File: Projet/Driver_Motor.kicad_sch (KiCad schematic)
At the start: 7 parts

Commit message: board_schematic
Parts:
- removed JP?: SolderJumper_2_Open, symbol Jumper:SolderJumper_2_Open
- added JP?: SolderJumper_2_Open, Jumper:SolderJumper-2_P1.3mm_Open_TrianglePad1.0x1.5mm, symbol Jumper:SolderJumper_2_Open
- JP3002: renamed from JP?; footprint (none) -> Jumper:SolderJumper-2_P1.3mm_Open_TrianglePad1.0x1.5mm
- gave numbers to parts that had none: 5
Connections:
- net +3.3V: now also U3001.3 (VDD)
- net V+_batterie: now also JP?.2 (B); no longer U3001.2 (VM)
- new net: JP?.1 (A), U3001.2 (VM)

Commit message: pcb_begin
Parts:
- removed JP?: SolderJumper_2_Open, Jumper:SolderJumper-2_P1.3mm_Open_TrianglePad1.0x1.5mm, symbol Jumper:SolderJumper_2_Open
- added JP302, JP303: SolderJumper_2_Open, Jumper:SolderJumper-2_P1.3mm_Open_TrianglePad1.0x1.5mm, symbol Jumper:SolderJumper_2_Open
- J301: renamed from J3001; footprint Connector_JST:JST_XH_B6B-XH-AM_1x06_P2.50mm_Vertical -> Connector_JST:JST_XH_B6B-XH-A_1x06_P2.50mm_Vertical
- J302: renamed from J3002; footprint Connector_JST:JST_XH_B6B-XH-AM_1x06_P2.50mm_Vertical -> Connector_JST:JST_XH_B6B-XH-A_1x06_P2.50mm_Vertical
- U301: renamed from U3001; footprint Package_SO:SOIC-8_3.9x4.9mm_P1.27mm -> Package_SO:SO-8_3.9x4.9mm_P1.27mm
- U302: renamed from U3002; footprint Package_SO:SOIC-8_3.9x4.9mm_P1.27mm -> Package_SO:SO-8_3.9x4.9mm_P1.27mm
- renumbered J3003 to J303, JP3002 to JP301
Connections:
- net +3.3V: now also JP302.2 (B); no longer U301.3 (VDD)
- net V+_batterie: now also JP303.2 (B)
- net at U301.2 (VM): now also JP303.1 (A)
- new net: JP302.1 (A), U301.3 (VDD)
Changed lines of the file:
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@@
     (stroke (width 0) (type default) (color 0 0 0 0))
   )
-  (wire (pts (xy 50.8 133.604) (xy 50.8 144.78))
+  (wire (pts (xy 50.8 133.604) (xy 50.8 135.128))
     (stroke (width 0) (type default) (color 0 0 0 0))
   )
@@
   )
   (wire (pts (xy 54.61 28.956) (xy 54.61 32.004))
+    (stroke (width 0) (type default) (color 0 0 0 0))
+  )
+  (wire (pts (xy 50.8 142.748) (xy 50.8 144.78))
     (stroke (width 0) (type default) (color 0 0 0 0))
   )
@@
   (symbol (lib_id "Connector_Generic:Conn_01x06") (at 114.3 50.8 0) (unit 1)
     (in_bom yes) (on_board yes) (fields_autoplaced)
-    (property "Reference" "J3002" (id 0) (at 116.84 50.7999 0)
+    (property "Reference" "J302" (id 0) (at 116.84 50.7999 0)
       (effects (font (size 1.27 1.27)) (justify left))
     )
@@
       (effects (font (size 1.27 1.27)) (justify left))
     )
-    (property "Footprint" "Connector_JST:JST_XH_B6B-XH-AM_1x06_P2.50mm_Vertical" (id 2) (at 114.3 50.8 0)
+    (property "Footprint" "Connector_JST:JST_XH_B6B-XH-A_1x06_P2.50mm_Vertical" (id 2) (at 114.3 50.8 0)
       (effects (font (size 1.27 1.27)) hide)
     )
@@
     (pin "6")
   )
+  (symbol (lib_id "Jumper:SolderJumper_2_Open") (at 55.88 135.382 90) (unit 1)
+    (in_bom yes) (on_board yes) (fields_autoplaced)
+    (property "Reference" "JP303" (id 0) (at 58.42 134.1119 90)
+      (effects (font (size 1.27 1.27)) (justify right))
+    )
+    (property "Value" "SolderJumper_2_Open" (id 1) (at 58.42 136.6519 90)
+      (effects (font (size 1.27 1.27)) (justify right))
+    )
+    (property "Footprint" "Jumper:SolderJumper-2_P1.3mm_Open_TrianglePad1.0x1.5mm" (id 2) (at 55.88 135.382 0)
+      (effects (font (size 1.27 1.27)) hide)
+    )
+    (property "Datasheet" "~" (id 3) (at 55.88 135.382 0)
+      (effects (font (size 1.27 1.27)) hide)
+    )
+    (pin "1")
+    (pin "2")
+  )
   (symbol (lib_id "power:GND") (at 57.15 59.69 0) (unit 1)
     (in_bom yes) (on_board yes) (fields_autoplaced)
-    (property "Reference" "#PWR0116" (id 0) (at 57.15 66.04 0)
+    (property "Reference" "#PWR0304" (id 0) (at 57.15 66.04 0)
       (effects (font (size 1.27 1.27)) hide)
     )
@@
   (symbol (lib_id "Driver_Motor:ZXBM5210-S") (at 53.34 154.94 0) (unit 1)
     (in_bom yes) (on_board yes) (fields_autoplaced)
-    (property "Reference" "U3001" (id 0) (at 55.3594 162.56 0)
+    (property "Reference" "U301" (id 0) (at 55.3594 162.56 0)
       (effects (font (size 1.27 1.27)) (justify left))
     )
@@
       (effects (font (size 1.27 1.27)) (justify left))
     )
-    (property "Footprint" "Package_SO:SOIC-8_3.9x4.9mm_P1.27mm" (id 2) (at 54.61 161.29 0)
+    (property "Footprint" "Package_SO:SO-8_3.9x4.9mm_P1.27mm" (id 2) (at 54.61 161.29 0)
       (effects (font (size 1.27 1.27)) hide)
     )
@@
   (symbol (lib_id "power:+3.3V") (at 101.6 55.88 90) (unit 1)
     (in_bom yes) (on_board yes) (fields_autoplaced)
-    (property "Reference" "#PWR0123" (id 0) (at 105.41 55.88 0)
+    (property "Reference" "#PWR0307" (id 0) (at 105.41 55.88 0)
       (effects (font (size 1.27 1.27)) hide)
     )
@@
   (symbol (lib_id "Driver_Motor:ZXBM5210-S") (at 57.15 52.07 0) (unit 1)
     (in_bom yes) (on_board yes) (fields_autoplaced)
-    (property "Reference" "U3002" (id 0) (at 59.1694 59.69 0)
+    (property "Reference" "U302" (id 0) (at 59.1694 59.69 0)
       (effects (font (size 1.27 1.27)) (justify left))
     )
@@
       (effects (font (size 1.27 1.27)) (justify left))
     )
-    (property "Footprint" "Package_SO:SOIC-8_3.9x4.9mm_P1.27mm" (id 2) (at 58.42 58.42 0)
+    (property "Footprint" "Package_SO:SO-8_3.9x4.9mm_P1.27mm" (id 2) (at 58.42 58.42 0)
       (effects (font (size 1.27 1.27)) hide)
     )
@@
   (symbol (lib_id "power:+3.3V") (at 92.71 160.02 90) (unit 1)
     (in_bom yes) (on_board yes) (fields_autoplaced)
-    (property "Reference" "#PWR0120" (id 0) (at 96.52 160.02 0)
+    (property "Reference" "#PWR0306" (id 0) (at 96.52 160.02 0)
       (effects (font (size 1.27 1.27)) hide)
     )
@@
     (pin "1")
   )
-  (symbol (lib_id "Jumper:SolderJumper_2_Open") (at 55.88 135.382 90) (unit 1)
-    (in_bom yes) (on_board yes) (fields_autoplaced)
-    (property "Reference" "JP?" (id 0) (at 58.42 134.1119 90)
-      (effects (font (size 1.27 1.27)) (justify right))
-    )
-    (property "Value" "SolderJumper_2_Open" (id 1) (at 58.42 136.6519 90)
-      (effects (font (size 1.27 1.27)) (justify right))
-    )
-    (property "Footprint" "Jumper:SolderJumper-2_P1.3mm_Open_TrianglePad1.0x1.5mm" (id 2) (at 55.88 135.382 0)
-      (effects (font (size 1.27 1.27)) hide)
-    )
-    (property "Datasheet" "~" (id 3) (at 55.88 135.382 0)
+  (symbol (lib_id "Jumper:SolderJumper_2_Open") (at 50.8 138.938 90) (unit 1)
+    (in_bom yes) (on_board yes) (fields_autoplaced)
+    (property "Reference" "JP302" (id 0) (at 53.34 137.6679 90)
+      (effects (font (size 1.27 1.27)) (justify right))
+    )
+    (property "Value" "SolderJumper_2_Open" (id 1) (at 53.34 140.2079 90)
+      (effects (font (size 1.27 1.27)) (justify right))
+    )
+    (property "Footprint" "Jumper:SolderJumper-2_P1.3mm_Open_TrianglePad1.0x1.5mm" (id 2) (at 50.8 138.938 0)
+      (effects (font (size 1.27 1.27)) hide)
+    )
+    (property "Datasheet" "~" (id 3) (at 50.8 138.938 0)
       (effects (font (size 1.27 1.27)) hide)
     )
@@
   (symbol (lib_id "power:GND") (at 102.87 48.26 270) (unit 1)
     (in_bom yes) (on_board yes) (fields_autoplaced)
-    (property "Reference" "#PWR0122" (id 0) (at 96.52 48.26 0)
+    (property "Reference" "#PWR0308" (id 0) (at 96.52 48.26 0)
       (effects (font (size 1.27 1.27)) hide)
     )
@@
   (symbol (lib_id "power:+3.3V") (at 54.61 28.956 0) (unit 1)
     (in_bom yes) (on_board yes) (fields_autoplaced)
-    (property "Reference" "#PWR0117" (id 0) (at 54.61 32.766 0)
+    (property "Reference" "#PWR0303" (id 0) (at 54.61 32.766 0)
       (effects (font (size 1.27 1.27)) hide)
     )
@@
   (symbol (lib_id "power:GND") (at 92.71 152.4 270) (unit 1)
     (in_bom yes) (on_board yes) (fields_autoplaced)
-    (property "Reference" "#PWR0115" (id 0) (at 86.36 152.4 0)
+    (property "Reference" "#PWR0305" (id 0) (at 86.36 152.4 0)
       (effects (font (size 1.27 1.27)) hide)
     )
@@
   (symbol (lib_id "Connector_Generic:Conn_01x06") (at 106.68 154.94 0) (unit 1)
     (in_bom yes) (on_board yes) (fields_autoplaced)
-    (property "Reference" "J3001" (id 0) (at 109.22 154.9399 0)
+    (property "Reference" "J301" (id 0) (at 109.22 154.9399 0)
       (effects (font (size 1.27 1.27)) (justify left))
     )
@@
       (effects (font (size 1.27 1.27)) (justify left))
     )
-    (property "Footprint" "Connector_JST:JST_XH_B6B-XH-AM_1x06_P2.50mm_Vertical" (id 2) (at 106.68 154.94 0)
+    (property "Footprint" "Connector_JST:JST_XH_B6B-XH-A_1x06_P2.50mm_Vertical" (id 2) (at 106.68 154.94 0)
       (effects (font (size 1.27 1.27)) hide)
     )
@@
   (symbol (lib_id "Connector_Generic:Conn_01x03") (at 199.39 95.25 0) (unit 1)
     (in_bom yes) (on_board yes) (fields_autoplaced)
-    (property "Reference" "J3003" (id 0) (at 201.93 93.9799 0)
+    (property "Reference" "J303" (id 0) (at 201.93 93.9799 0)
       (effects (font (size 1.27 1.27)) (justify left))
     )
@@
   (symbol (lib_id "power:GND") (at 194.31 92.71 270) (unit 1)
     (in_bom yes) (on_board yes) (fields_autoplaced)
-    (property "Reference" "#PWR0121" (id 0) (at 187.96 92.71 0)
+    (property "Reference" "#PWR0309" (id 0) (at 187.96 92.71 0)
       (effects (font (size 1.27 1.27)) hide)
     )
@@
   (symbol (lib_id "Jumper:SolderJumper_2_Open") (at 54.61 35.814 90) (unit 1)
     (in_bom yes) (on_board yes) (fields_autoplaced)
-    (property "Reference" "JP3002" (id 0) (at 57.15 34.5439 90)
+    (property "Reference" "JP301" (id 0) (at 57.15 34.5439 90)
       (effects (font (size 1.27 1.27)) (justify right))
     )
@@
   (symbol (lib_id "power:GND") (at 53.34 162.56 0) (unit 1)
     (in_bom yes) (on_board yes) (fields_autoplaced)
-    (property "Reference" "#PWR0118" (id 0) (at 53.34 168.91 0)
+    (property "Reference" "#PWR0302" (id 0) (at 53.34 168.91 0)
       (effects (font (size 1.27 1.27)) hide)
     )
@@
   (symbol (lib_id "power:+3.3V") (at 50.8 133.604 0) (unit 1)
     (in_bom yes) (on_board yes) (fields_autoplaced)
-    (property "Reference" "#PWR0119" (id 0) (at 50.8 137.414 0)
-      (effects (font (size 1.27 1.27)) hide)
-    )
+    (property "Reference" "#PWR0301" (id 0) (at 50.8 137.414 0)
+      (effects (font (size 1.27 1.27)) hide)
+    )

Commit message: placement
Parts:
- added C301: 100uF, Capacitor_THT:CP_Radial_D6.3mm_P2.50mm, symbol Device:C_Polarized_Small
- added C302: 0.1uF, Capacitor_SMD:C_0603_1608Metric_Pad1.08x0.95mm_HandSolder, symbol Device:C_Small
- added C303, C304: 1uF, Capacitor_SMD:C_0603_1608Metric_Pad1.08x0.95mm_HandSolder, symbol Device:C_Small
- added C305, C306: 100nF, Capacitor_SMD:C_0603_1608Metric_Pad1.08x0.95mm_HandSolder, symbol Device:C_Small
- added R301: 10k, Resistor_SMD:R_0603_1608Metric_Pad0.98x0.95mm_HandSolder, symbol Device:R_Small
- J303: footprint Connector_JST:JST_XH_S3B-XH-A_1x03_P2.50mm_Horizontal -> Connector_JST:JST_XH_B3B-XH-A_1x03_P2.50mm_Vertical
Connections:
- net +3.3V: now also R301.2
- net GND: now also C301.2, C302.1, C303.2, C304.2, C305.2, C306.2
- net SERV_DATA: now also R301.1
- net V+_batterie: now also C301.1, C302.2, C306.1
- net at JP303.1 (A), U301.2 (VM): now also C305.1
- net at JP302.1 (A), U301.3 (VDD): now also C303.1
- net at JP301.1 (A), U302.3 (VDD): now also C304.1
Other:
- moved on the sheet: JP303

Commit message: Routing
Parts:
- added C307, C308, C309, C310: 1uF, Capacitor_SMD:C_0603_1608Metric_Pad1.08x0.95mm_HandSolder, symbol Device:C_Small
- added JP304: SolderJumper_2_Open, Jumper:SolderJumper-2_P1.3mm_Open_TrianglePad1.0x1.5mm, symbol Jumper:SolderJumper_2_Open
- C305, C306: value 100nF -> 10uF
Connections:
- net +3.3V: no longer JP301.2 (B), JP302.2 (B)
- net GND: now also C307.1, C308.1, C309.1, C310.1
- net M1+: now also C310.2
- net M1-: now also C308.2
- net M2+: now also C309.2
- net M2-: now also C307.2
- net V+_batterie: now also JP304.2 (B); no longer C306.1, U302.2 (VM)
- new net: C306.1, JP304.1 (A), U302.2 (VM)
- new net +5V: JP301.2 (B), JP302.2 (B)
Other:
- note added: "Capacités 100 nF, recommandé pour faible courant"
- moved on the sheet: C301, C302, J301, J302

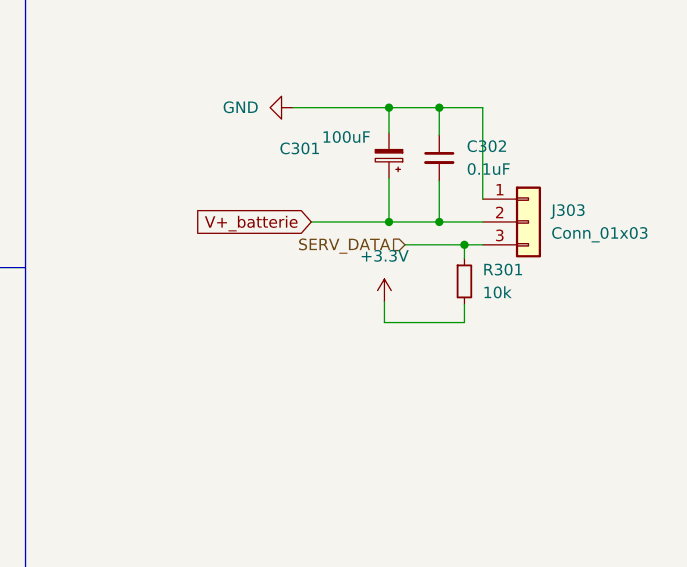
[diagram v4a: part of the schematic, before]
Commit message: PCB_ROUTAGE_Modif
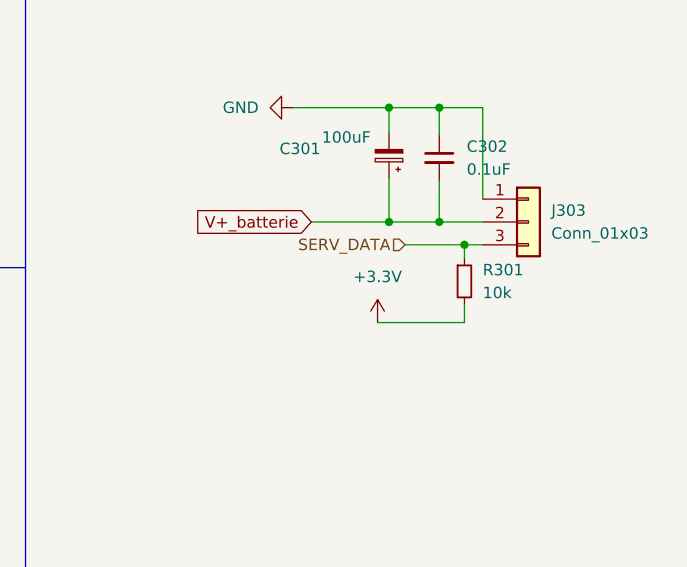
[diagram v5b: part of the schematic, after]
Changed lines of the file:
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@@
-    (stroke (width 0) (type default) (color 0 0 0 0))
-  )
-  (wire (pts (xy 183.388 106.426) (xy 183.388 104.14))
     (stroke (width 0) (type default) (color 0 0 0 0))
   )
@@
     (stroke (width 0) (type default) (color 0 0 0 0))
   )
-  (wire (pts (xy 183.388 106.426) (xy 192.278 106.426))
+  (wire (pts (xy 182.626 106.426) (xy 192.278 106.426))
     (stroke (width 0) (type default) (color 0 0 0 0))
   )
@@
     (pin "2")
   )
-  (symbol (lib_id "power:+3.3V") (at 183.388 104.14 0) (unit 1)
-    (in_bom yes) (on_board yes) (fields_autoplaced)
-    (property "Reference" "#PWR0106" (id 0) (at 183.388 107.95 0)
-      (effects (font (size 1.27 1.27)) hide)
-    )
-    (property "Value" "+3.3V" (id 1) (at 183.388 99.06 0))
-    (property "Footprint" "" (id 2) (at 183.388 104.14 0)
-      (effects (font (size 1.27 1.27)) hide)
-    )
-    (property "Datasheet" "" (id 3) (at 183.388 104.14 0)
-      (effects (font (size 1.27 1.27)) hide)
-    )
+  (symbol (lib_id "power:+3.3V") (at 182.626 106.426 0) (unit 1)
+    (in_bom yes) (on_board yes) (fields_autoplaced)
+    (property "Reference" "#PWR0106" (id 0) (at 182.626 110.236 0)
+      (effects (font (size 1.27 1.27)) hide)
+    )
+    (property "Value" "+3.3V" (id 1) (at 182.626 101.346 0))
+    (property "Footprint" "" (id 2) (at 182.626 106.426 0)
+      (effects (font (size 1.27 1.27)) hide)
+    )
+    (property "Datasheet" "" (id 3) (at 182.626 106.426 0)
+      (effects (font (size 1.27 1.27)) hide)
+    )

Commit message: Routage_fini
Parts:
- added JP305, JP306, JP307, JP308: SolderJumper_2_Open, Jumper:SolderJumper-2_P1.3mm_Open_TrianglePad1.0x1.5mm, symbol Jumper:SolderJumper_2_Open
- J301: value Moteur 1 -> Moteur 2
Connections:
- net +3.3V: no longer J301.5 (Pin_5), J302.5 (Pin_5)
- net +5V: now also J301.5 (Pin_5), J302.5 (Pin_5)
- net M1+: now also JP308.2 (B); no longer C310.2, U302.1 (OUT1)
- net M1-: now also JP307.2 (B); no longer C308.2, U302.7 (OUT2)
- net M2+: now also JP305.2 (B); no longer C309.2, U301.1 (OUT1)
- net M2-: now also JP306.2 (B); no longer C307.2, U301.7 (OUT2)
- net VM_DRIVER_2_JP: now reaches C305.1, JP303.1 (A), U301.2 (VM)
- net 5V_DRV_2: now reaches C303.1, JP302.1 (A), U301.3 (VDD)
- net VM_DRIVER_1_JP: now reaches C306.1, JP304.1 (A), U302.2 (VM)
- net 5V_DRV_1: now reaches C304.1, JP301.1 (A), U302.3 (VDD)
- new net M1+_JP: C310.2, JP308.1 (A), U302.1 (OUT1)
- new net M1-_JP: C308.2, JP307.1 (A), U302.7 (OUT2)
- new net M2+_JP: C309.2, JP305.1 (A), U301.1 (OUT1)
- new net M2-_JP: C307.2, JP306.1 (A), U301.7 (OUT2)
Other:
- moved on the sheet: C307, C308, C309, C310
